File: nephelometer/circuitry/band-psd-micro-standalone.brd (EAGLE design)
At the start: 88 x 54 mm, 69 parts, among them IC1 LMC6484P, IC2 LM555N, IC3 74HCT74N, IC4 4044N, IC8 7805TV, T1 2N2222, T2 2N2222, U1 MAX4544, U4 MotA

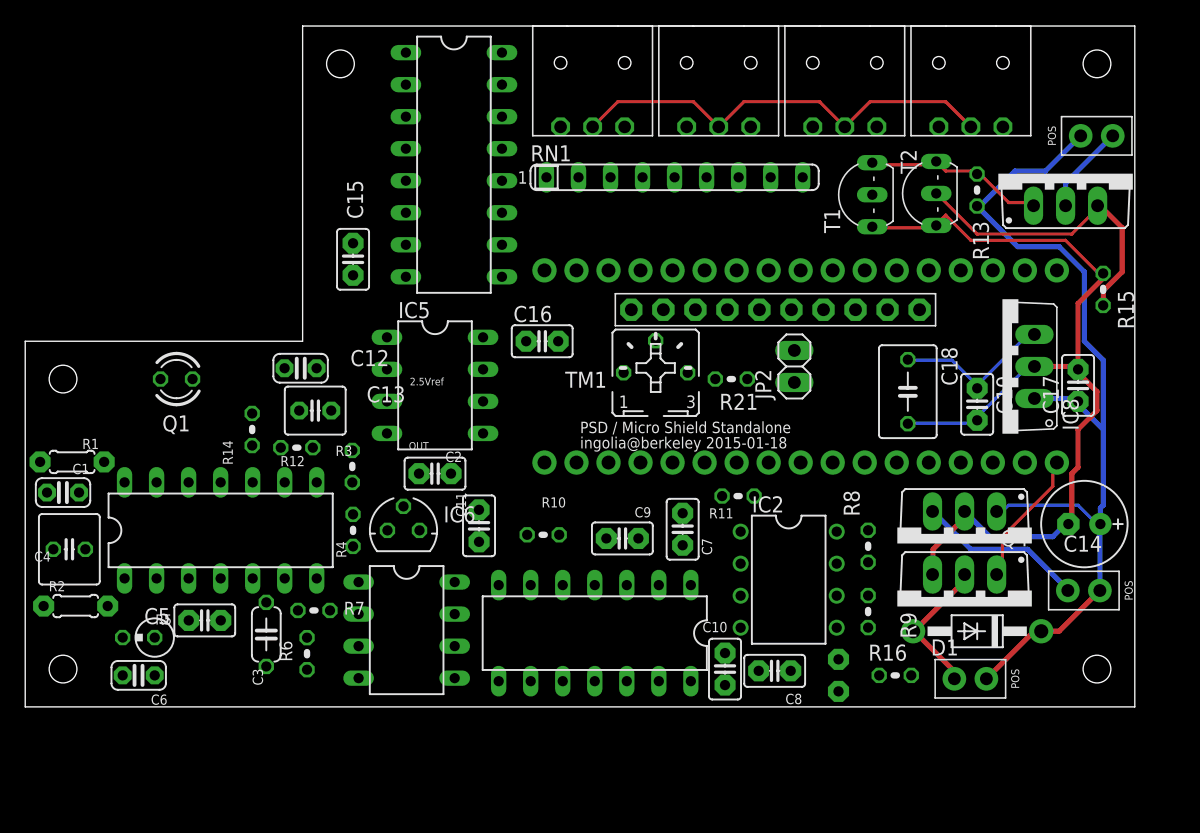
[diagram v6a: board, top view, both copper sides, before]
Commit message: Routed most of board except push-buttons and latch
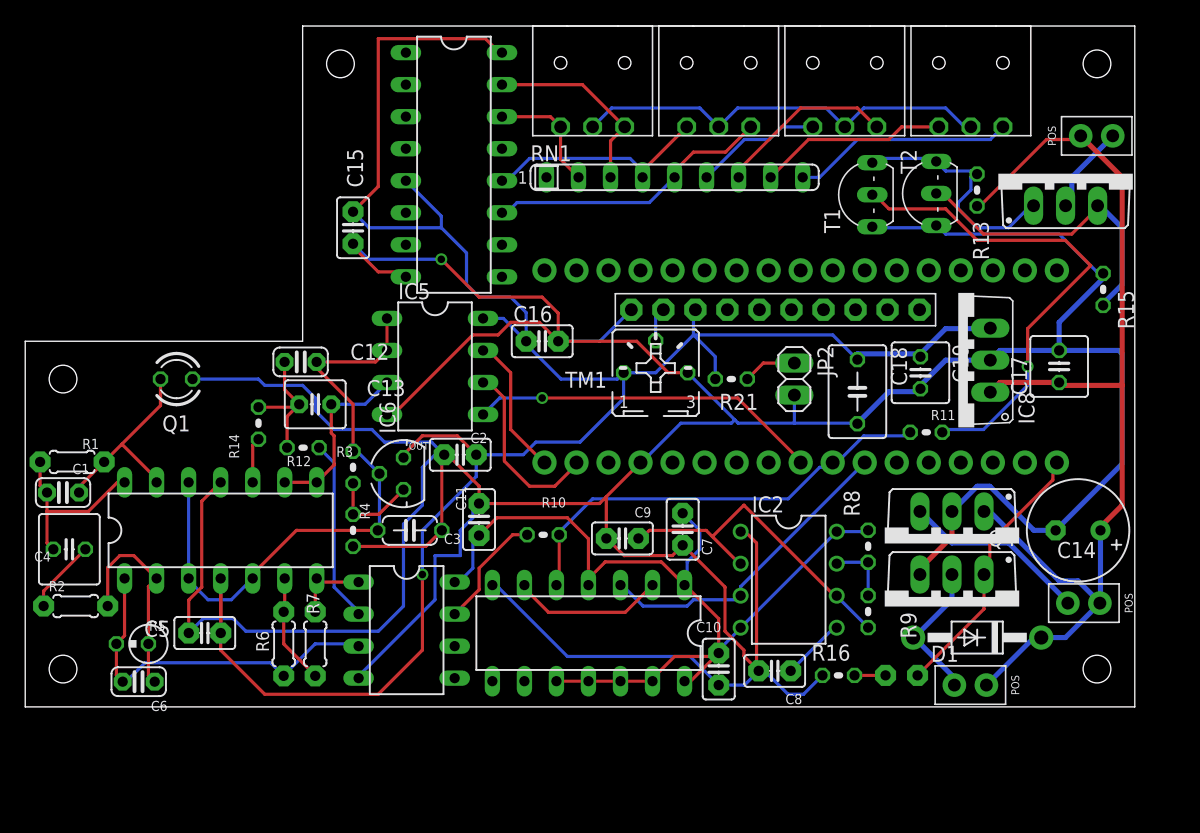
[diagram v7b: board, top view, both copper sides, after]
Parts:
- C14: value 100µ -> 220µF; device adafruit:E2,5-7 -> adafruit:E3,5-8
- C17, C19: device adafruit:C025-025X050 -> adafruit:C025-050X050
- D1: value 1N4004 -> 1N4935
- R6, R7: device adafruit:0204V -> adafruit:0204/5
- moved R11 15.8 mm to (71.5, 27.8), turned to 0 degrees
- moved C3 14.1 mm to (30.5, 20.0), turned to 0 degrees
- moved C19 5.15 mm to (71.0, 32.5)
- moved LED1 5.00 mm to (69.5, 8.50), turned to 0 degrees
- moved IC6 4.50 mm to (30.0, 24.5), turned to 90 degrees
- moved R16 4.50 mm to (64.5, 8.50)
- moved C18 4.00 mm to (66.0, 31.0)
- moved IC8 3.54 mm to (74.0, 33.5)
- moved R7 2.65 mm to (23.0, 11.0), turned to 90 degrees
- moved C15 2.50 mm to (26.0, 44.0)
- moved C2 2.50 mm to (34.5, 26.0)
- moved C17 2.12 mm to (82.0, 33.0)
- moved R6 2.01 mm to (20.5, 11.0)
- moved IC5 1.50 mm to (32.5, 33.0)
- moved C5 1.00 mm to (14.2, 11.9)
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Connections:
- net +5V: now also IC3.10, IC3.11, IC3.12, IC3.13
- net N$33: now also RN1.3; no longer RN1.2
- net N$34: now also RN1.2; no longer RN1.3
- net N$36: now also RN1.5; no longer RN1.4
- net N$37: now also RN1.4; no longer RN1.5
- net N$40: now also RN1.6; no longer RN1.7
- net N$42: now also RN1.9; no longer RN1.8
- net N$43: now also RN1.8; no longer RN1.9
- net N$44: now also RN1.7; no longer RN1.6
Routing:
- net GND: track 109.6 -> 392.8 mm, vias 0 -> 1
- net +5V: track 13.4 -> 246.2 mm, vias 0 -> 1
- net 2.5V: track 0.00 -> 50.1 mm
- net LEDCTRL: track 0.00 -> 39.8 mm, vias 0 -> 1
- net 5KHZ: track 0.00 -> 35.6 mm
- net N$26: track 0.00 -> 29.6 mm
- net CS_ADC: track 0.00 -> 27.9 mm, vias 0 -> 1
- net N$9: track 0.00 -> 26.8 mm
- net 10KHZ: track 0.00 -> 25.2 mm
- net N$36: track 0.00 -> 22.8 mm
- net N$37: track 0.00 -> 18.2 mm
- net N$42: track 0.00 -> 17.5 mm
- net N$25: track 0.00 -> 16.7 mm
- net N$1: track 0.00 -> 15.8 mm
- net N$33: track 0.00 -> 15.6 mm
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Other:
- board text removed: "2.5Vref"
- board text removed: "PSD / Micro Shield Standalone ingolia@berkeley 2015-01-18"
- board text removed: "V0"
- board text removed: "Vdd"
- board text removed: "Vss"

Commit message: Finished routing traces, all DRC okay
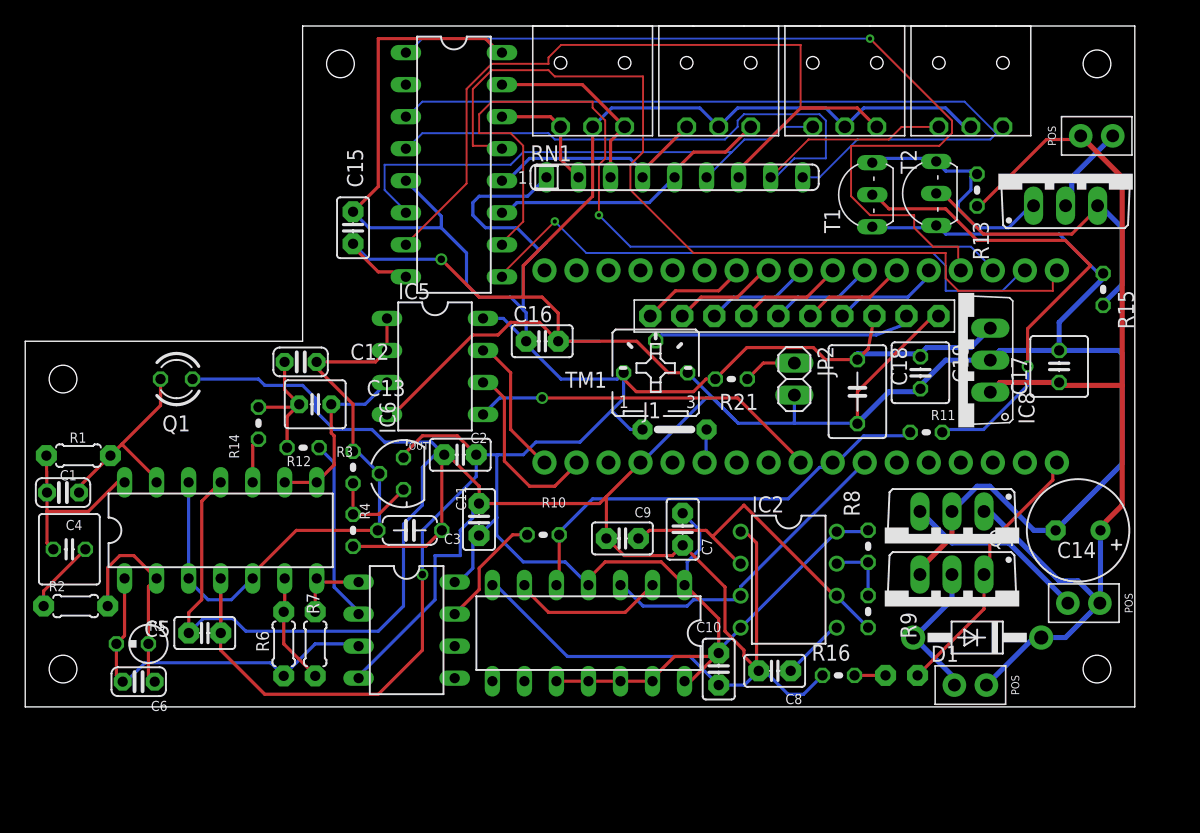
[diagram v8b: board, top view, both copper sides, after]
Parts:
- added J1: J5MM, jumper:05
- moved 16X2 1.58 mm to (61.0, 37.0), turned to 180 degrees
- moved R1 0.71 mm to (4.22, 25.9)
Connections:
- removed net N$30 (its old number): 16X2.8, U3.P$7
- new net N$20: 16X2.10, U3.P$11
- new net N$31: 16X2.6, U3.P$7
- net +5V: now also J1.1
- net N$24: now also 16X2.9, U3.P$10; no longer 16X2.10, U3.P$5
- net N$29: now also 16X2.8, U3.P$9; no longer 16X2.9, U3.P$6
- net N$32: now also 16X2.5, U3.P$6; no longer 16X2.6, U3.P$9
- net N$41: now also 16X2.4, U3.P$5; no longer 16X2.5, U3.P$10
- net N$46: now also J1.2, U3.P$23; no longer 16X2.4, U3.P$11
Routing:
- net N$39: track 0.00 -> 72.5 mm, vias 0 -> 1
- net N$15: track 0.00 -> 70.5 mm
- net N$45: track 0.00 -> 66.1 mm, vias 0 -> 1
- net N$42: track 17.5 -> 66.6 mm
- net N$44: track 14.3 -> 61.8 mm
- net N$11: track 0.00 -> 47.5 mm, vias 0 -> 1
- net N$43: track 15.0 -> 58.3 mm
- net N$40: track 10.1 -> 42.5 mm
- net +5V: track 246.2 -> 271.9 mm
- net GND: track 392.8 -> 418.1 mm
- net N$38: track 2.71 -> 20.9 mm
- net N$41: track 0.00 -> 8.62 mm
- net N$20: track 0.00 -> 8.47 mm
- net N$29: track 0.00 -> 8.42 mm
- net N$30: track 0.00 -> 8.40 mm
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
